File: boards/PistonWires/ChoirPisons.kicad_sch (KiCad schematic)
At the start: 30 parts, among them J5 ChoirLEDs, J6 ChoirPistons, SW49 SW, SW50 SW, SW51 SW, SW52 SW, SW53 SW, SW54 SW, SW55 SW, SW56 SW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

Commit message: Renamed PCBs and updated to KiCAD 7.0
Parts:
- gave numbers to parts that had none: 10

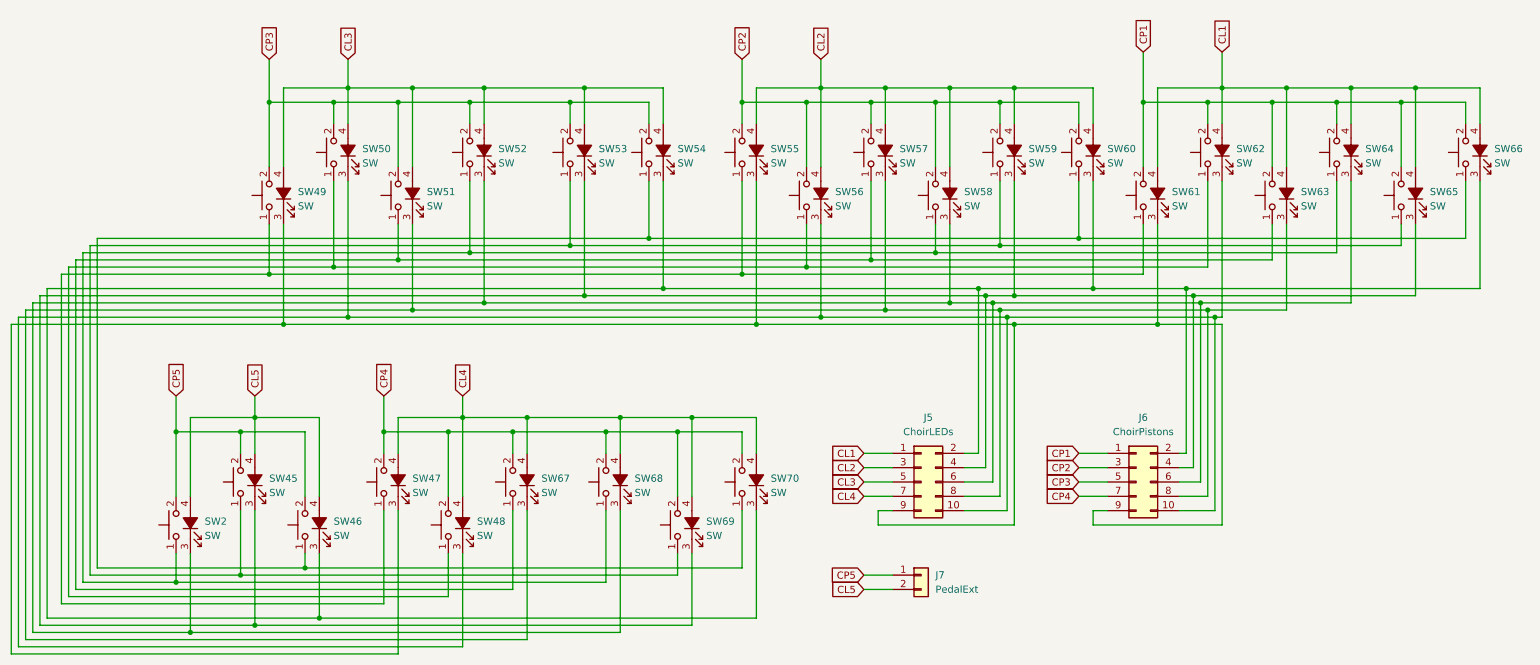
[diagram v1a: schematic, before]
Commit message: Updated to KiCAD 8, fixed optocouplers for MIDI and added powersupplies
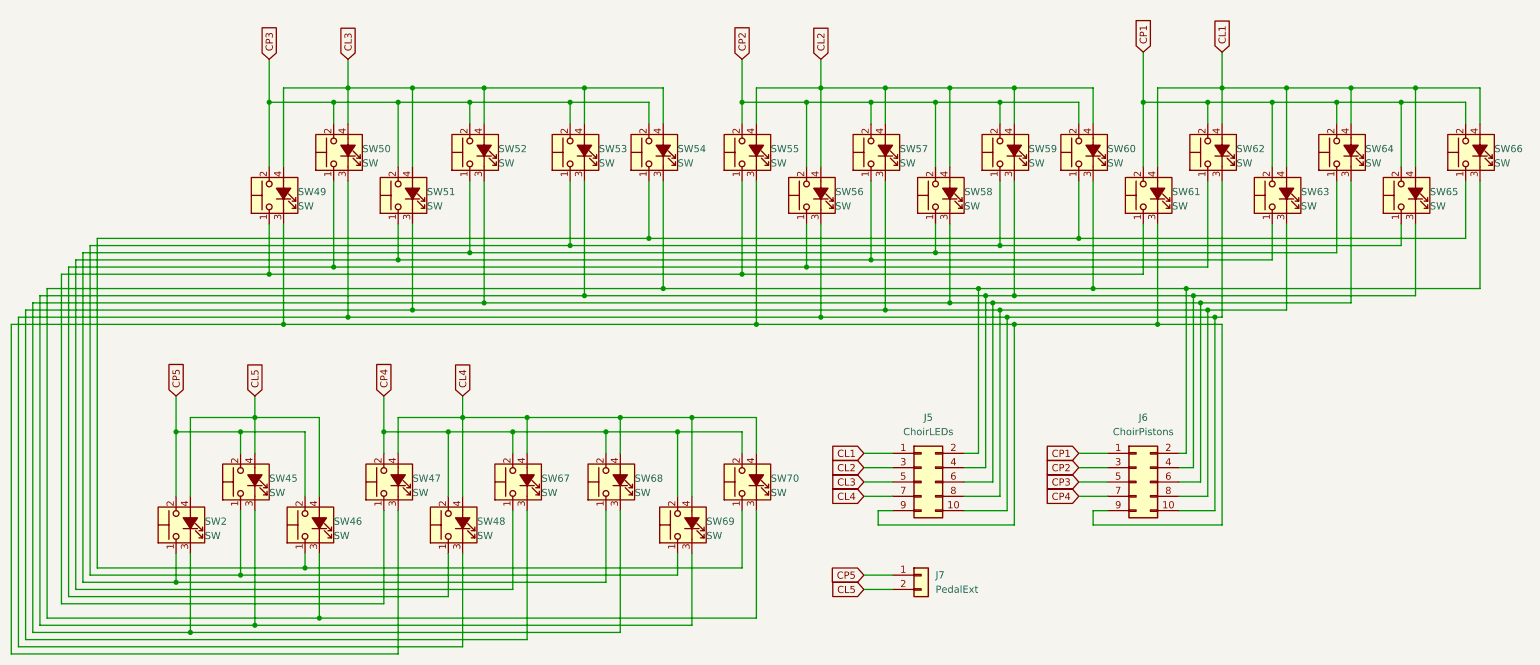
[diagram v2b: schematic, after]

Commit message: Fixed Piston wiring schematics, updated I2C message formats
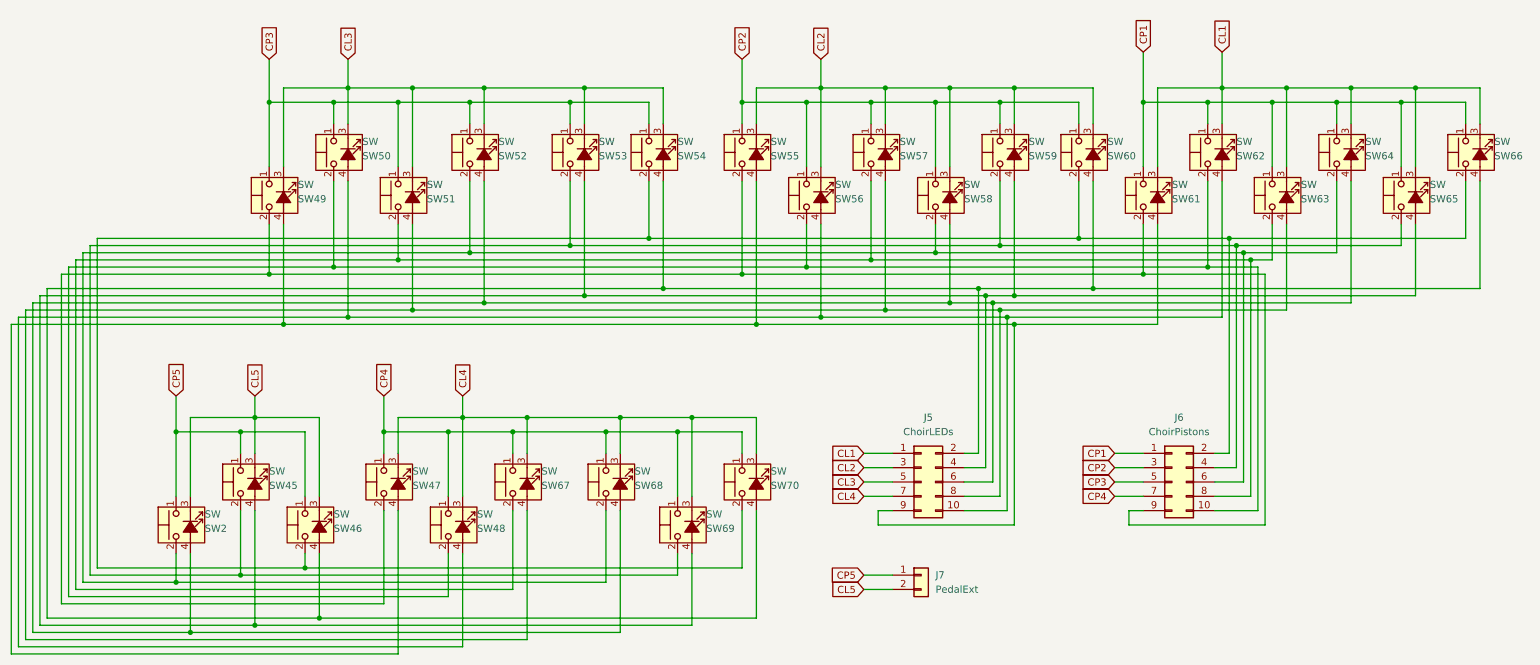
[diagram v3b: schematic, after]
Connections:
- net CL1: now also SW61.3 (K), SW62.3 (K), SW63.3 (K), SW64.3 (K), SW65.3 (K), SW66.3 (K); no longer SW61.4 (A), SW62.4 (A), SW63.4 (A), SW64.4 (A), SW65.4 (A), SW66.4 (A)
- net CL2: now also SW55.3 (K), SW56.3 (K), SW57.3 (K), SW58.3 (K), SW59.3 (K), SW60.3 (K); no longer SW55.4 (A), SW56.4 (A), SW57.4 (A), SW58.4 (A), SW59.4 (A), SW60.4 (A)
- net CL3: now also SW49.3 (K), SW50.3 (K), SW51.3 (K), SW52.3 (K), SW53.3 (K), SW54.3 (K); no longer SW49.4 (A), SW50.4 (A), SW51.4 (A), SW52.4 (A), SW53.4 (A), SW54.4 (A)
- net CL4: now also SW47.3 (K), SW48.3 (K), SW67.3 (K), SW68.3 (K), SW69.3 (K), SW70.3 (K); no longer SW47.4 (A), SW48.4 (A), SW67.4 (A), SW68.4 (A), SW69.4 (A), SW70.4 (A)
- net CL5: now also SW2.3 (K), SW45.3 (K), SW46.3 (K); no longer SW2.4 (A), SW45.4 (A), SW46.4 (A)
- net CP1: now also SW61.1, SW62.1, SW63.1, SW64.1, SW65.1, SW66.1; no longer SW61.2, SW62.2, SW63.2, SW64.2, SW65.2, SW66.2
- net CP2: now also SW55.1, SW56.1, SW57.1, SW58.1, SW59.1, SW60.1; no longer SW55.2, SW56.2, SW57.2, SW58.2, SW59.2, SW60.2
- net CP3: now also SW49.1, SW50.1, SW51.1, SW52.1, SW53.1, SW54.1; no longer SW49.2, SW50.2, SW51.2, SW52.2, SW53.2, SW54.2
- net CP4: now also SW47.1, SW48.1, SW67.1, SW68.1, SW69.1, SW70.1; no longer SW47.2, SW48.2, SW67.2, SW68.2, SW69.2, SW70.2
- net CP5: now also SW2.1, SW45.1, SW46.1; no longer SW2.2, SW45.2, SW46.2
- new net: J6.6 (Pin_6), SW2.2, SW52.2, SW58.2, SW64.2, SW68.2
- new net: J5.6 (Pin_6), SW2.4 (A), SW52.4 (A), SW58.4 (A), SW64.4 (A), SW68.4 (A)
- new net: J6.8 (Pin_8), SW51.2, SW57.2, SW63.2, SW67.2
- new net: J5.8 (Pin_8), SW51.4 (A), SW57.4 (A), SW63.4 (A), SW67.4 (A)
- new net: J6.9 (Pin_9), SW47.2, SW49.2, SW55.2, SW61.2
- new net: J5.9 (Pin_9), SW47.4 (A), SW49.4 (A), SW55.4 (A), SW61.4 (A)
- new net: J6.4 (Pin_4), SW45.2, SW53.2, SW59.2, SW65.2, SW69.2
- new net: J5.4 (Pin_4), SW45.4 (A), SW53.4 (A), SW59.4 (A), SW65.4 (A), SW69.4 (A)
- new net: J6.10 (Pin_10), SW48.2, SW50.2, SW56.2, SW62.2
- new net: J5.10 (Pin_10), SW48.4 (A), SW50.4 (A), SW56.4 (A), SW62.4 (A)
- new net: J6.2 (Pin_2), SW46.2, SW54.2, SW60.2, SW66.2, SW70.2
- new net: J5.2 (Pin_2), SW46.4 (A), SW54.4 (A), SW60.4 (A), SW66.4 (A), SW70.4 (A)
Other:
- moved on the sheet: J6
